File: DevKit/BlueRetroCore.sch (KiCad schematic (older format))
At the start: 105 parts, among them J1 USB_C_Receptacle_USB2.0, J2 Conn_02x13, J3 Micro_SD_Card, J4 Conn_01x03, J5 DB25_Female_MountingHoles, J6 Conn_02x13, Q1 BSS138, Q2 BSS138, Q3 S8050, Q4 S8050, Q5 S8050, SW1 BOOT, SW2 EN, U1 ESP32-WROOM, U10 TPD6F003, U11 TPD6F003, U12 TPD6F003, U13 TPD6F003, U2 FT2232HL, U3 STL6N3LLH6, U4 TCPP01-M12, U5 M93C46, U6 ECMF02-2AMX6, U7 TPD6F003, U8 AP7361C-33E, U9 AP7361C-33E, Y1 12MHz

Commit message: Basic placement PCB
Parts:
- added D11: RED_RA, BlueRetro:LED_0605_1611Metric, symbol BlueRetro:LED
- added J7: Conn_02x07, BlueRetro:PinHeader_2x07_P2.54mm_Vertical, symbol BlueRetro:Conn_02x07_Odd_Even
- added R36: 64.9, BlueRetro:R_0402_1005Metric, symbol BlueRetro:R_US
- D6: value GREEN -> GREEN_RA; footprint BlueRetro:LED_0603_1608Metric -> BlueRetro:LED_0605_1611Metric; DigiKey Part Number 160-1446-2-ND -> 846-1157-1-ND; Manufacturer_Part_Number LTST-C191KGKT -> SML-A12M8TT86
- J2: value Conn_02x13 -> Conn_02x06; footprint BlueRetro:PinHeader_2x13_P2.54mm_Vertical -> BlueRetro:PinHeader_2x06_P2.54mm_Vertical; symbol BlueRetro:Conn_02x13_Odd_Even -> BlueRetro:Conn_02x06_Odd_Even
- J3: symbol BlueRetro:Micro_SD_Card -> BlueRetro:Micro_SD_Card_Det
- J4: DigiKey Part Number S1011EC-40-ND -> (none); Manufacturer_Part_Number PRPC040SAAN-RC -> (none)
- J6: footprint BlueRetro:PinHeader_2x13_P2.54mm_Vertical -> BlueRetro:PinHeader_2x13_P2.54mm_Vertical_TB; DigiKey Part Number S2011EC-40-ND -> (none); Manufacturer_Part_Number PRPC040DAAN-RC -> (none)
- R26, R27: value 64.9 -> 150; DigiKey Part Number RMCF0402FT64R9CT-ND -> P150LCT-ND; Manufacturer_Part_Number RMCF0402FT64R9 -> ERJ-2RKF1500X
- U3: Arrow Part Number STL6N3LLH6 -> (none); Arrow Price/Stock https://www.arrow.com/en/products/stl6n3llh6/stmicroelectro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 -> (none); Description STMicroelectronics STL6N3LLH6 N-channel MOSFET Transistor, 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 -> (none); Manufacturer_Name STMicroelectronics -> (none); Mouser Part Number 511-STL6N3LLH6 -> (none); Mouser Price/Stock https://www.mouser.co.uk/ProductDetail/STMicroelectronics/S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 -> (none)
- U4: Arrow Part Number TCPP01-M12 -> (none); Arrow Price/Stock https://www.arrow.com/en/products/tcpp01-m12/stmicroelectro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 -> (none); Description USB type-C port protection -> (none); Height 1 -> (none); Manufacturer_Name STMicroelectronics -> (none); Mouser Part Number 511-TCPP01-M12 -> (none); Mouser Price/Stock https://www.mouser.co.uk/ProductDetail/STMicroelectronics/T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 -> (none)
- U6: Arrow Part Number ECMF02-2AMX6 -> (none); Arrow Price/Stock https://www.arrow.com/en/products/ecmf02-2amx6/stmicroelect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 -> (none); Description Common Mode Filter & ESD Prot. USB uQFN6 STMicroelectronics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 -> (none); Height 0.55 -> (none); Manufacturer_Name STMicroelectronics -> (none); Mouser Part Number 511-ECMF02-2AMX6 -> (none); Mouser Price/Stock https://www.mouser.co.uk/ProductDetail/STMicroelectronics/E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 -> (none)
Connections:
- net +3V3: now also J2.1 (Pin_1), J2.2 (Pin_2)
- net +3V3_USB: now also J7.1 (Pin_1), J7.2 (Pin_2); no longer J2.1 (Pin_1), J2.2 (Pin_2)
- net EN: now also J7.11 (Pin_11); no longer J2.21 (Pin_21)
- net GND: now also J3.11 (SHIELD), D11.1 (K), J7.13 (Pin_13), J7.14 (Pin_14); no longer J2.23 (Pin_23), J2.24 (Pin_24), J2.25 (Pin_25), J2.26 (Pin_26), J3.9 (SHIELD)
- net IO12: now also J7.5 (Pin_5); no longer J2.15 (Pin_15)
- net IO13: now also J7.3 (Pin_3); no longer J2.13 (Pin_13)
- net IO14: now also J7.9 (Pin_9); no longer J2.19 (Pin_19)
- net IO15: now also J7.7 (Pin_7); no longer J2.17 (Pin_17)
- net IO17: now also R36.1
- net TCK: now also J7.4 (Pin_4); no longer J2.14 (Pin_14)
- net TDI: now also J7.6 (Pin_6); no longer J2.16 (Pin_16)
- net TDO: now also J7.8 (Pin_8); no longer J2.18 (Pin_18)
- net TMS: now also J7.10 (Pin_10); no longer J2.20 (Pin_20)
- net nTRST: now also J7.12 (Pin_12); no longer J2.22 (Pin_22)
- new net: D11.2 (A), R36.2
- no-connect marks 38 -> 40
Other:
- moved on the sheet: C22, C23, Q1, Q2, R23, R24, R25, R28, R31, R32, SW1, SW2

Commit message: PCB routing
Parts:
- removed R29, R30: 0, BlueRetro:R_0603_1608Metric, symbol BlueRetro:R_0P
- removed U1: ESP32-WROOM, BlueRetro:ESP32-WROOM-32, symbol BlueRetro:ESP32-WROOM
- added U1: ESP32-WROOM-32E, BlueRetro:ESP32-WROOM-32, symbol BlueRetro:ESP32-WROOM-32E
- H1, H2, H3, H4: footprint BlueRetro:MountingHole_3.2mm_M3 -> BlueRetro:MountingHole_2.7mm_M2.5
- U8, U9: footprint BlueRetro:SOT-223-3_TabPin2 -> BlueRetro:SOT-223-3_TabPin3
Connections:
- net EN: now also J7.3 (Pin_3), U1.3 (EN); no longer J7.11 (Pin_11)
- net GND: now also U8.2 (GND), U9.2 (GND), U1.1 (GND), U1.15 (GND), U1.38 (GND)
- net I34: now also U12.2 (Ch2_In), U1.6 (IO34); no longer U12.6 (Ch6_In)
- net I34_C: now also J5.10, J6.10 (Pin_10), U12.11 (Ch2_Out); no longer J5.12, J6.12 (Pin_12), U12.7 (Ch6_Out)
- net I35: now also U12.3 (Ch3_In), U1.7 (IO35); no longer U13.2 (Ch2_In)
- net I35_C: now also J5.23 (P23), J6.23 (Pin_23), U12.10 (Ch3_Out); no longer J5.13, J6.13 (Pin_13), U13.11 (Ch2_Out)
- net I36: now also U11.6 (Ch6_In), U1.4 (SENSOR_VP); no longer U12.5 (Ch5_In)
- net I36_C: now also J5.21 (P21), J6.21 (Pin_21), U11.7 (Ch6_Out); no longer J5.24 (P24), J6.24 (Pin_24), U12.8 (Ch5_Out)
- net I39: now also U12.1 (Ch1_In), U1.5 (SENSOR_VN); no longer U13.1 (Ch1_In)
- net I39_C: now also J5.22 (P22), J6.22 (Pin_22), U12.12 (Ch1_Out); no longer J5.25 (P25), J6.25 (Pin_25), U13.12 (Ch1_Out)
- net IO0: now also U11.5 (Ch5_In), U1.25 (IO0); no longer U10.2 (Ch2_In)
- net IO0_C: now also J5.20 (P20), J6.20 (Pin_20), U11.8 (Ch5_Out); no longer J5.14 (P14), J6.14 (Pin_14), U10.11 (Ch2_Out)
- net IO1: now also U10.3 (Ch3_In), U1.35 (TXD0); no longer U10.4 (Ch4_In)
- net IO12: now also J7.11 (Pin_11), U7.6 (Ch6_In), U1.14 (IO12); no longer J7.5 (Pin_5), U7.1 (Ch1_In)
- net IO13: now also J7.9 (Pin_9), U7.5 (Ch5_In), U1.16 (IO13); no longer J7.3 (Pin_3), U7.2 (Ch2_In)
- net IO14: now also J7.5 (Pin_5), U7.3 (Ch3_In), U1.13 (IO14); no longer J7.9 (Pin_9), U7.4 (Ch4_In)
- net IO15: now also U7.4 (Ch4_In), U1.23 (IO15); no longer U7.3 (Ch3_In)
- net IO16: now also U11.4 (Ch4_In), U1.27 (IO16); no longer U11.3 (Ch3_In)
- net IO16_C: now also J5.19 (P19), J6.19 (Pin_19), U11.9 (Ch4_Out); no longer J5.18 (P18), J6.18 (Pin_18), U11.10 (Ch3_Out)
- net IO17: now also U11.3 (Ch3_In), U1.28 (IO17); no longer U11.4 (Ch4_In)
- net IO17_C: now also J5.18 (P18), J6.18 (Pin_18), U11.10 (Ch3_Out); no longer J5.19 (P19), J6.19 (Pin_19), U11.9 (Ch4_Out)
- net IO18: now also U11.1 (Ch1_In), U1.30 (IO18); no longer U11.5 (Ch5_In)
- net IO18_C: now also J5.4, J6.4 (Pin_4), U11.12 (Ch1_Out); no longer J5.20 (P20), J6.20 (Pin_20), U11.8 (Ch5_Out)
- net IO19: now also U10.6 (Ch6_In), U1.31 (IO19); no longer U10.1 (Ch1_In)
- net IO19_C: now also J5.16 (P16), J6.16 (Pin_16), U10.7 (Ch6_Out); no longer J5.1, J6.1 (Pin_1), U10.12 (Ch1_Out)
- net IO1_C: now also J5.2, J6.2 (Pin_2), U10.10 (Ch3_Out); no longer J5.15 (P15), J6.15 (Pin_15), U10.9 (Ch4_Out)
- net IO2: now also U7.2 (Ch2_In), U1.24 (IO2); no longer U7.5 (Ch5_In)
- net IO21: now also U10.5 (Ch5_In), U1.33 (IO21); no longer U10.3 (Ch3_In)
- net IO21_C: now also J5.3, J6.3 (Pin_3), U10.8 (Ch5_Out); no longer J5.2, J6.2 (Pin_2), U10.10 (Ch3_Out)
- net IO22: now also U10.2 (Ch2_In), U1.36 (IO22); no longer U10.5 (Ch5_In)
- net IO22_C: now also J5.14 (P14), J6.14 (Pin_14), U10.11 (Ch2_Out); no longer J5.3, J6.3 (Pin_3), U10.8 (Ch5_Out)
- net IO23: now also U10.1 (Ch1_In), U1.37 (IO23); no longer U11.6 (Ch6_In)
- net IO23_C: now also J5.1, J6.1 (Pin_1), U10.12 (Ch1_Out); no longer J5.21 (P21), J6.21 (Pin_21), U11.7 (Ch6_Out)
- net IO25: now also U12.6 (Ch6_In), U1.10 (IO25); no longer U11.1 (Ch1_In)
- net IO25_C: now also J5.12, J6.12 (Pin_12), U12.7 (Ch6_Out); no longer J5.4, J6.4 (Pin_4), U11.12 (Ch1_Out)
- net IO26: now also U13.1 (Ch1_In), U1.11 (IO26); no longer U12.1 (Ch1_In)
- net IO26_C: now also J5.25 (P25), J6.25 (Pin_25), U13.12 (Ch1_Out); no longer J5.22 (P22), J6.22 (Pin_22), U12.12 (Ch1_Out)
- net IO27: now also U13.2 (Ch2_In), U1.12 (IO27); no longer U12.3 (Ch3_In)
- net IO27_C: now also J5.13, J6.13 (Pin_13), U13.11 (Ch2_Out); no longer J5.23 (P23), J6.23 (Pin_23), U12.10 (Ch3_Out)
- net IO3: now also U10.4 (Ch4_In), U1.34 (RXD0); no longer U10.6 (Ch6_In)
- net IO32: now also U12.4 (Ch4_In), U1.8 (IO32); no longer U12.2 (Ch2_In)
- net IO32_C: now also J5.11, J6.11 (Pin_11), U12.9 (Ch4_Out); no longer J5.10, J6.10 (Pin_10), U12.11 (Ch2_Out)
- net IO33: now also U12.5 (Ch5_In), U1.9 (IO33); no longer U12.4 (Ch4_In)
- net IO33_C: now also J5.24 (P24), J6.24 (Pin_24), U12.8 (Ch5_Out); no longer J5.11, J6.11 (Pin_11), U12.9 (Ch4_Out)
- net IO3_C: now also J5.15 (P15), J6.15 (Pin_15), U10.9 (Ch4_Out); no longer J5.16 (P16), J6.16 (Pin_16), U10.7 (Ch6_Out)
- net IO4: now also U7.1 (Ch1_In), U1.26 (IO4); no longer U7.6 (Ch6_In)
- net IO5: now also U1.29 (IO5)
- net TCK: now also J7.10 (Pin_10); no longer J7.4 (Pin_4)
- net TDI: now also J7.12 (Pin_12); no longer J7.6 (Pin_6)
- net TMS: now also J7.6 (Pin_6); no longer J7.10 (Pin_10)
- net nTRST: now also J7.4 (Pin_4); no longer J7.12 (Pin_12)
- net at R2.1: now also U1.2 (3V3)
- net USB_N: now reaches U2.7 (DM), U6.2 (D_2)
- net USB_P: now reaches U2.8 (DP), U6.1 (D_1)
- net USB_C_N: now reaches J1.A7 (D-), J1.B7 (D-), U6.5 (D-)
- net USB_C_P: now reaches J1.A6 (D+), J1.B6 (D+), U6.6 (D+)
- net at J3.1 (DAT2): now also U7.7 (Ch6_Out); no longer U7.12 (Ch1_Out)
- net at J3.2 (DAT3/CD): now also U7.8 (Ch5_Out); no longer U7.11 (Ch2_Out)
- net at J3.3 (CMD): now also U7.9 (Ch4_Out); no longer U7.10 (Ch3_Out)
- net at J3.5 (CLK): now also U7.10 (Ch3_Out); no longer U7.9 (Ch4_Out)
- net at J3.7 (DAT0): now also U7.11 (Ch2_Out); no longer U7.8 (Ch5_Out)
- net at J3.8 (DAT1): now also U7.12 (Ch1_Out); no longer U7.7 (Ch6_Out)
- net at U4.5 (GATE): now also U3.3 (G); no longer U3.4 (S_1)
- net at D2.1 (K), D3.2 (A), J1.A4 (VBUS)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: now also U3.1 (D_1), U3.2 (D_2); no longer U3.8 (S_2)
- new net: D1.2 (A), U3.4 (S_1), U3.8 (S_2), U4.4 (SOURCE)
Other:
- moved on the sheet: C15, C5, C6, D1, R1, R2, U7

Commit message: Update schematic & BOM
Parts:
- U1: DigiKey Part Number (none) -> 1965-ESP32-WROOM-32E(4MB)CT-ND; Manufacturer_Part_Number (none) -> ESP32-WROOM-32E (4MB)
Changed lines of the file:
@@
 F 2 "BlueRetro:ESP32-WROOM-32" H 4950 4800 60  0001 C CNN
 F 3 "" H 4150 3900 60  0001 C CNN
+F 4 "1965-ESP32-WROOM-32E(4MB)CT-ND" H 4600 3450 50  0001 C CNN "DigiKey Part Number"
+F 5 "ESP32-WROOM-32E (4MB)" H 4600 3450 50  0001 C CNN "Manufacturer_Part_Number"
 	1    4600 3450
 	1    0    0    -1

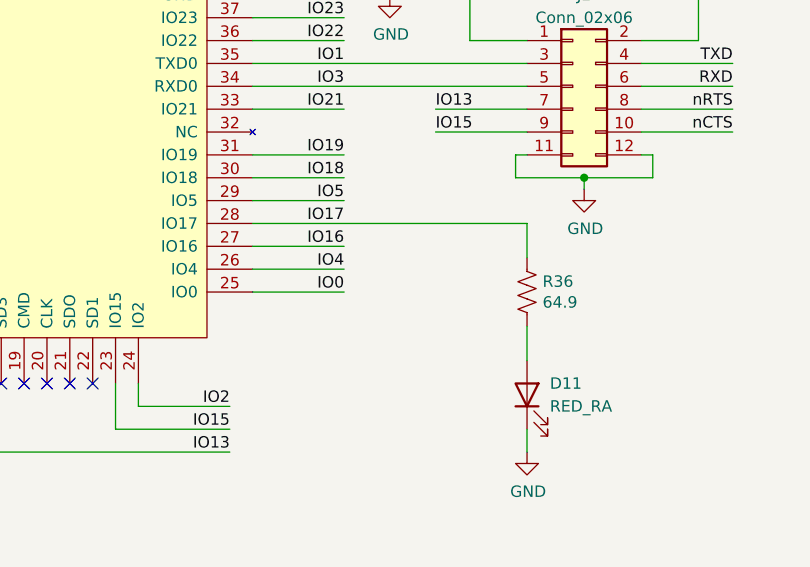
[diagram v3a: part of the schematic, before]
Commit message: LED is on by default at boot and shutdown by software
This allow to detect bootloader/flash issue
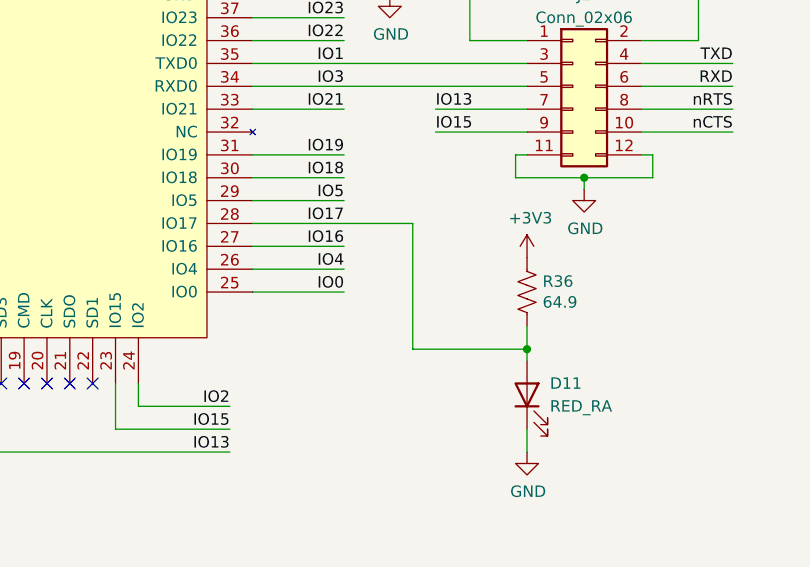
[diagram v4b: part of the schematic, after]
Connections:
- net +3V3: now also R36.1
- net IO17: now also D11.2 (A), R36.2; no longer R36.1
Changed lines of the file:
@@
 	6700 4850 6700 4750
 Wire Wire Line
-	6700 4450 6700 4300
+	6700 4450 6700 4400
 Wire Wire Line
 	5500 3950 5900 3950
-Wire Wire Line
-	5500 3850 6700 3850
-Wire Wire Line
-	6700 3850 6700 4000
 $Comp
 L BlueRetro:Conn_02x07_Odd_Even J7
@@
 Wire Wire Line
 	4200 7450 4400 7450
+Wire Wire Line
+	6700 4400 6200 4400
+Wire Wire Line
+	6200 4400 6200 3850
+Wire Wire Line
+	6200 3850 5500 3850
+Connection ~ 6700 4400
+Wire Wire Line
+	6700 4400 6700 4300
+$Comp
+L BlueRetro:+3V3 #PWR?
+U 1 1 5F4893B6
+P 6700 4000
+F 0 "#PWR?" H 6700 3850 50  0001 C CNN
+F 1 "+3V3" H 6715 4173 50  0000 C CNN
+F 2 "" H 6700 4000 50  0001 C CNN
+F 3 "" H 6700 4000 50  0001 C CNN
+	1    6700 4000
+	1    0    0    -1
+$EndComp
 $EndSCHEMATC

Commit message: Fix missing DB25 in BOM
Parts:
- J5: value DB25_Female_MountingHoles -> DB25_Female; symbol BlueRetro:DB25_Female_MountingHoles -> BlueRetro:DB25_Female_MH
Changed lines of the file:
@@
 $EndComp
 $Comp
-L BlueRetro:DB25_Female_MountingHoles J5
+L BlueRetro:DB25_Female_MH J5
 U 1 1 5F316A7E
 P 2350 11750
 F 0 "J5" H 2268 13242 50  0000 C CNN
-F 1 "DB25_Female_MountingHoles" H 2268 13151 50  0000 C CNN
+F 1 "DB25_Female" H 2268 13151 50  0000 C CNN
 F 2 "BlueRetro:DSUB-25_Female_Horizontal_P2.77x2.84mm_EdgePinOffset8.1mm_Housed_MountingHolesOffset9.5mm" H 2350 11750 50  0001 C CNN
 F 3 "~" H 2350 11750 50  0001 C CNN
@@
 	6700 4400 6700 4300
 $Comp
-L BlueRetro:+3V3 #PWR?
+L BlueRetro:+3V3 #PWR0103
 U 1 1 5F4893B6
 P 6700 4000
-F 0 "#PWR?" H 6700 3850 50  0001 C CNN
+F 0 "#PWR0103" H 6700 3850 50  0001 C CNN
 F 1 "+3V3" H 6715 4173 50  0000 C CNN
 F 2 "" H 6700 4000 50  0001 C CNN

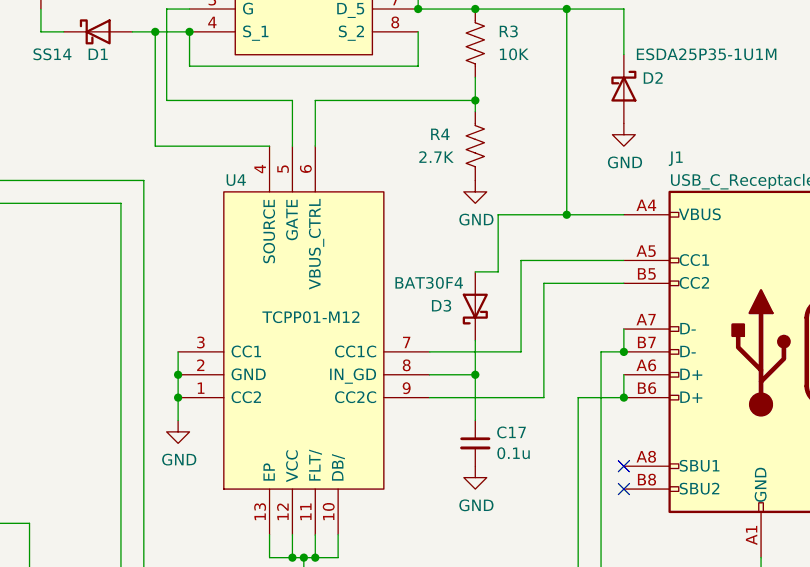
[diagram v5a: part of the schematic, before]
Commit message: Replace D3 with a bigger alternative
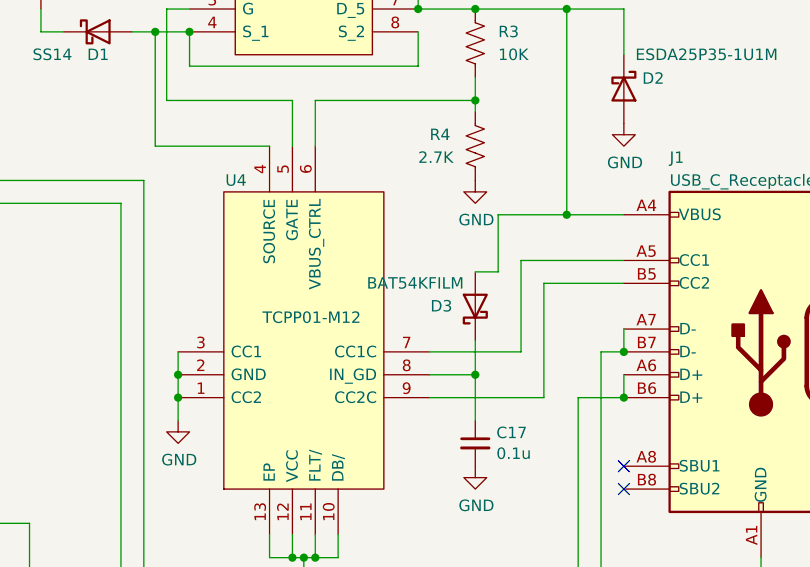
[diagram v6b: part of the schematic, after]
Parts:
- D3: value BAT30F4 -> BAT54KFILM; footprint BlueRetro:D_0201_0603Metric -> BlueRetro:D_SOD-523; DigiKey Part Number 497-15253-2-ND -> 497-5561-1-ND; Manufacturer_Part_Number BAT30F4 -> BAT54KFILM
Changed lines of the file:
@@
 P 18700 4750
 F 0 "D3" V 18700 4850 50  0000 L CNN
-F 1 "BAT30F4" V 18800 4800 50  0000 L CNN
-F 2 "BlueRetro:D_0201_0603Metric" H 18700 4750 50  0001 C CNN
+F 1 "BAT54KFILM" V 18800 4800 50  0000 L CNN
+F 2 "BlueRetro:D_SOD-523" H 18700 4750 50  0001 C CNN
 F 3 "~" H 18700 4750 50  0001 C CNN
-F 4 "497-15253-2-ND" H 18700 4750 50  0001 C CNN "DigiKey Part Number"
-F 5 "BAT30F4" H 18700 4750 50  0001 C CNN "Manufacturer_Part_Number"
+F 4 "497-5561-1-ND" H 18700 4750 50  0001 C CNN "DigiKey Part Number"
+F 5 "BAT54KFILM" H 18700 4750 50  0001 C CNN "Manufacturer_Part_Number"
 	1    18700 4750
 	0    -1   -1   0

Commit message: Fix SOT-223 Tab
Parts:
- U8, U9: footprint BlueRetro:SOT-223-3_TabPin3 -> BlueRetro:SOT-223-3_TabPin2
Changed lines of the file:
@@
 F 0 "U8" H 10600 9892 50  0000 C CNN
 F 1 "AP7361C-33E" H 10600 9801 50  0000 C CNN
-F 2 "BlueRetro:SOT-223-3_TabPin3" H 10600 9875 50  0001 C CIN
+F 2 "BlueRetro:SOT-223-3_TabPin2" H 10600 9875 50  0001 C CIN
 F 3 "~" H 10600 9600 50  0001 C CNN
 F 4 "AP7361C-33E-13DITR-ND" H 10600 9650 50  0001 C CNN "DigiKey Part Number"
@@
 F 0 "U9" H 12650 9892 50  0000 C CNN
 F 1 "AP7361C-33E" H 12650 9801 50  0000 C CNN
-F 2 "BlueRetro:SOT-223-3_TabPin3" H 12650 9875 50  0001 C CIN
+F 2 "BlueRetro:SOT-223-3_TabPin2" H 12650 9875 50  0001 C CIN
 F 3 "~" H 12650 9600 50  0001 C CNN
 F 4 "AP7361C-33E-13DITR-ND" H 12650 9650 50  0001 C CNN "DigiKey Part Number"

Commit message: PCB revision v1.1
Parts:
- U10, U11, U12, U13, U7: value TPD6F003 -> TPD6F002DSVR; footprint BlueRetro:Texas_R-PWSON-N12_EP0.4x2mm -> BlueRetro:Texas_DVS_R-PWSON-N12; DigiKey Part Number 296-25802-2-ND -> 296-25456-1-ND; Manufacturer_Part_Number TPD6F003DQDR -> TPD6F002DSVR
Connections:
- net IO1: now also J2.5 (Pin_5); no longer J2.3 (Pin_3)
- net IO3: now also J2.3 (Pin_3); no longer J2.5 (Pin_5)
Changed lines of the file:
@@
 P 4200 8100
 F 0 "U7" H 4200 8667 50  0000 C CNN
-F 1 "TPD6F003" H 4200 8576 50  0000 C CNN
-F 2 "BlueRetro:Texas_R-PWSON-N12_EP0.4x2mm" H 4150 7550 50  0001 C CNN
+F 1 "TPD6F002DSVR" H 4200 8576 50  0000 C CNN
+F 2 "BlueRetro:Texas_DVS_R-PWSON-N12" H 4150 7550 50  0001 C CNN
 F 3 "~" H 4350 7450 50  0001 C CNN
-F 4 "296-25802-2-ND" H 4200 8100 50  0001 C CNN "DigiKey Part Number"
-F 5 "TPD6F003DQDR" H 4200 8100 50  0001 C CNN "Manufacturer_Part_Number"
+F 4 "296-25456-1-ND" H 4200 8100 50  0001 C CNN "DigiKey Part Number"
+F 5 "TPD6F002DSVR" H 4200 8100 50  0001 C CNN "Manufacturer_Part_Number"
 	1    4200 8100
 	1    0    0    1
@@
 P 5450 10900
 F 0 "U10" H 5450 11467 50  0000 C CNN
-F 1 "TPD6F003" H 5450 11376 50  0000 C CNN
-F 2 "BlueRetro:Texas_R-PWSON-N12_EP0.4x2mm" H 5400 10350 50  0001 C CNN
+F 1 "TPD6F002DSVR" H 5450 11376 50  0000 C CNN
+F 2 "BlueRetro:Texas_DVS_R-PWSON-N12" H 5400 10350 50  0001 C CNN
 F 3 "~" H 5600 10250 50  0001 C CNN
-F 4 "296-25802-2-ND" H 5450 10900 50  0001 C CNN "DigiKey Part Number"
-F 5 "TPD6F003DQDR" H 5450 10900 50  0001 C CNN "Manufacturer_Part_Number"
+F 4 "296-25456-1-ND" H 5450 10900 50  0001 C CNN "DigiKey Part Number"
+F 5 "TPD6F002DSVR" H 5450 10900 50  0001 C CNN "Manufacturer_Part_Number"
 	1    5450 10900
 	-1   0    0    -1
@@
 P 5450 12300
 F 0 "U11" H 5450 12867 50  0000 C CNN
-F 1 "TPD6F003" H 5450 12776 50  0000 C CNN
-F 2 "BlueRetro:Texas_R-PWSON-N12_EP0.4x2mm" H 5400 11750 50  0001 C CNN
+F 1 "TPD6F002DSVR" H 5450 12776 50  0000 C CNN
+F 2 "BlueRetro:Texas_DVS_R-PWSON-N12" H 5400 11750 50  0001 C CNN
 F 3 "~" H 5600 11650 50  0001 C CNN
-F 4 "296-25802-2-ND" H 5450 12300 50  0001 C CNN "DigiKey Part Number"
-F 5 "TPD6F003DQDR" H 5450 12300 50  0001 C CNN "Manufacturer_Part_Number"
+F 4 "296-25456-1-ND" H 5450 12300 50  0001 C CNN "DigiKey Part Number"
+F 5 "TPD6F002DSVR" H 5450 12300 50  0001 C CNN "Manufacturer_Part_Number"
 	1    5450 12300
 	-1   0    0    -1
@@
 P 5450 13700
 F 0 "U12" H 5450 14267 50  0000 C CNN
-F 1 "TPD6F003" H 5450 14176 50  0000 C CNN
-F 2 "BlueRetro:Texas_R-PWSON-N12_EP0.4x2mm" H 5400 13150 50  0001 C CNN
+F 1 "TPD6F002DSVR" H 5450 14176 50  0000 C CNN
+F 2 "BlueRetro:Texas_DVS_R-PWSON-N12" H 5400 13150 50  0001 C CNN
 F 3 "~" H 5600 13050 50  0001 C CNN
-F 4 "296-25802-2-ND" H 5450 13700 50  0001 C CNN "DigiKey Part Number"
-F 5 "TPD6F003DQDR" H 5450 13700 50  0001 C CNN "Manufacturer_Part_Number"
+F 4 "296-25456-1-ND" H 5450 13700 50  0001 C CNN "DigiKey Part Number"
+F 5 "TPD6F002DSVR" H 5450 13700 50  0001 C CNN "Manufacturer_Part_Number"
 	1    5450 13700
 	-1   0    0    -1
@@
 P 5450 15100
 F 0 "U13" H 5450 15667 50  0000 C CNN
-F 1 "TPD6F003" H 5450 15576 50  0000 C CNN
-F 2 "BlueRetro:Texas_R-PWSON-N12_EP0.4x2mm" H 5400 14550 50  0001 C CNN
+F 1 "TPD6F002DSVR" H 5450 15576 50  0000 C CNN
+F 2 "BlueRetro:Texas_DVS_R-PWSON-N12" H 5400 14550 50  0001 C CNN
 F 3 "~" H 5600 14450 50  0001 C CNN
-F 4 "296-25802-2-ND" H 5450 15100 50  0001 C CNN "DigiKey Part Number"
-F 5 "TPD6F003DQDR" H 5450 15100 50  0001 C CNN "Manufacturer_Part_Number"
+F 4 "296-25456-1-ND" H 5450 15100 50  0001 C CNN "DigiKey Part Number"
+F 5 "TPD6F002DSVR" H 5450 15100 50  0001 C CNN "Manufacturer_Part_Number"
 	1    5450 15100
 	-1   0    0    -1
@@
 	6650 3550 6700 3550
 Connection ~ 6950 3650
-Wire Wire Line
-	5500 3150 6700 3150
-Wire Wire Line
-	5500 3250 6700 3250
 $Comp
 L BlueRetro:+3V3 #PWR0101
@@
 	1    0    0    -1
 $EndComp
+Wire Wire Line
+	5500 3150 5900 3150
+Wire Wire Line
+	5500 3250 5900 3250
+Wire Wire Line
+	6700 3150 6300 3150
+Wire Wire Line
+	6700 3250 6300 3250
+Text Label 6300 3250 0    50   ~ 0
+IO1
+Text Label 6300 3150 0    50   ~ 0
+IO3
 $EndSCHEMATC
